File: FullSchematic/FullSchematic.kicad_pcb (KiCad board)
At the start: 2 copper layers, 91.4 x 81.3 mm, 59 parts, among them IC1 TTP223E-BA6, J1 USB_B_Micro, J2 TP4056, P1 Touch Pad, Q1 PMOS, U1 LM1117-3.3, U2 CH340C, U3 24LC64, U4 STM32F051C6T6

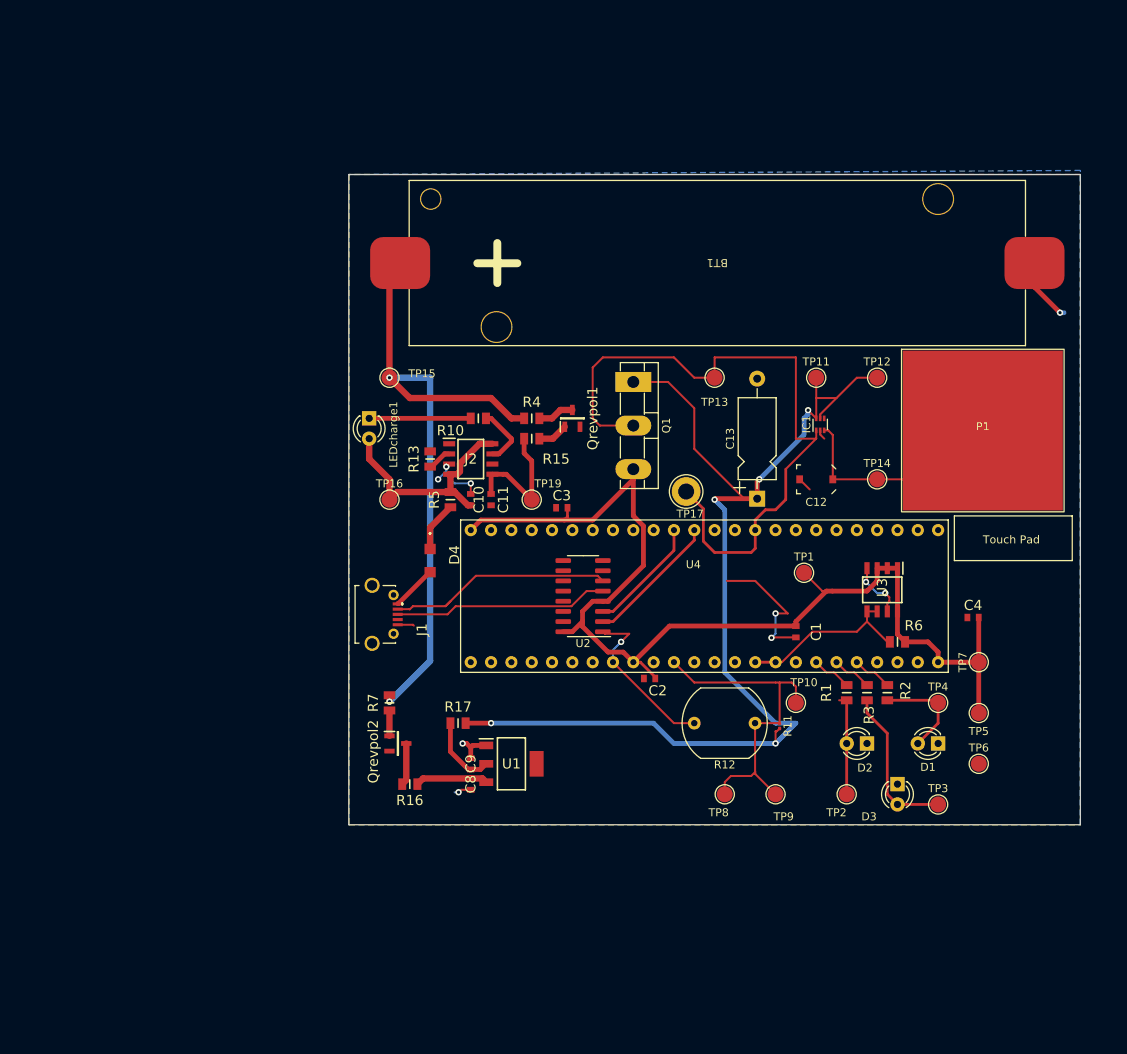
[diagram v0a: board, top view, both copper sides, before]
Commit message: Added uvlo circuit
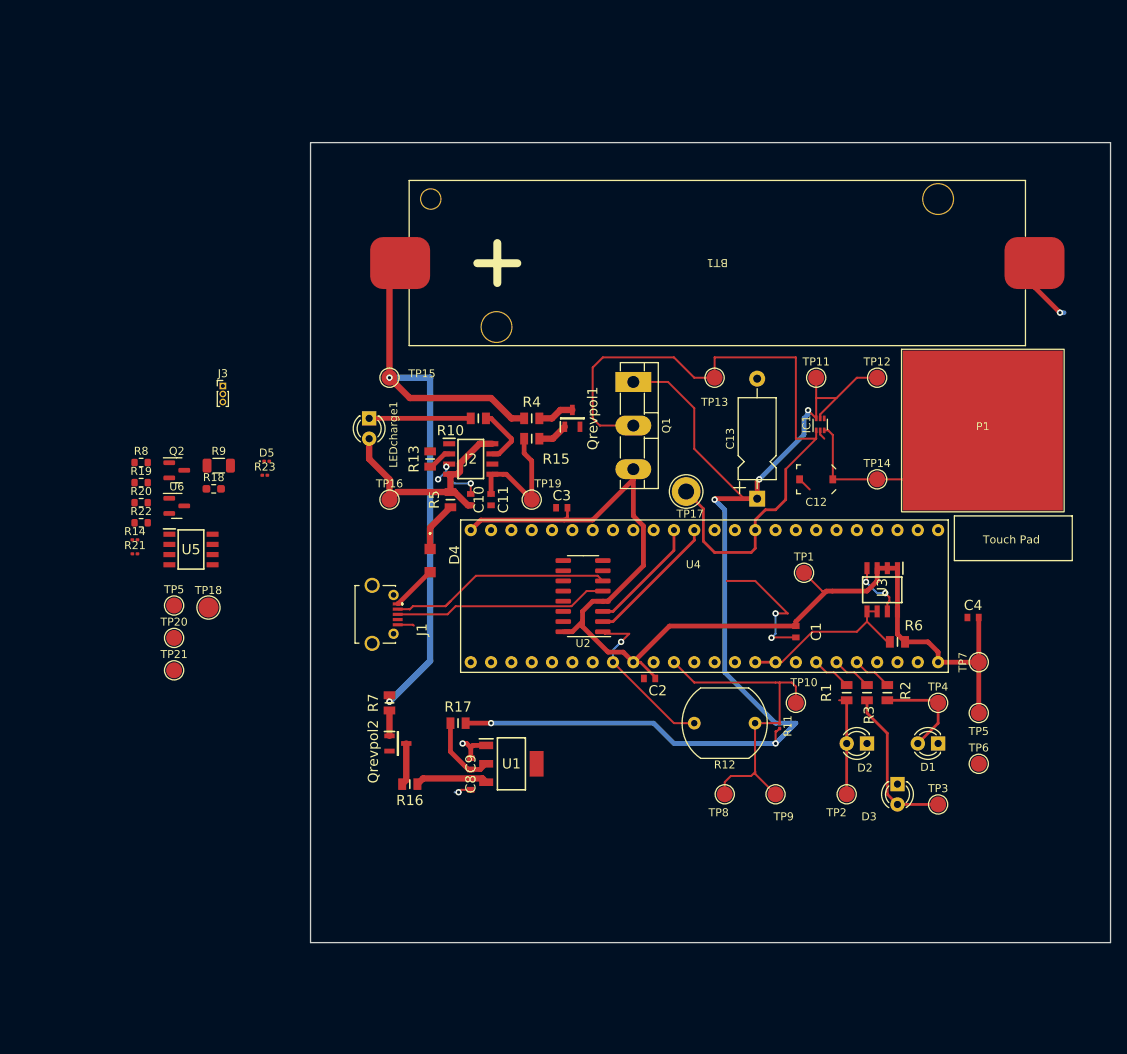
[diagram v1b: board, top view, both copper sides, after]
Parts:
- added D5: LED, LED_SMD:LED_0201_0603Metric, F.Cu at (71.0, 86.6)
- added J3: Conn_01x03_Pin, Connector_PinHeader_1.00mm:PinHeader_1x03_P1.00mm_Vertical, F.Cu at (65.5, 77.2)
- added Q2: IRLML6402, Package_TO_SOT_SMD:SOT-23, F.Cu at (59.8, 87.8)
- added R14: 1M, Resistor_SMD:R_0201_0603Metric, F.Cu at (54.5, 96.5)
- added R18: 10M, Resistor_SMD:R_0603_1608Metric_Pad0.98x0.95mm_HandSolder, F.Cu at (64.4, 90.1)
- added R19: 150k, Resistor_SMD:R_0603_1608Metric, F.Cu at (55.3, 89.3)
- added R20: 2.05M, Resistor_SMD:R_0603_1608Metric, F.Cu at (55.3, 91.8)
- added R21: 100k, Resistor_SMD:R_0201_0603Metric, F.Cu at (54.5, 98.2)
- added R22: 2M, Resistor_SMD:R_0603_1608Metric, F.Cu at (55.3, 94.3)
- added R23: 150, Resistor_SMD:R_0201_0603Metric, F.Cu at (70.8, 88.4)
- added R8: 2M, Resistor_SMD:R_0603_1608Metric, F.Cu at (55.3, 86.8)
- added R9: 2.5M, Resistor_SMD:R_1206_3216Metric, F.Cu at (65.0, 87.2)
- added TP18: TestPoint, TestPoint:TestPoint_Pad_D2.5mm, F.Cu at (63.7, 104.9)
- added TP20: TestPoint, TestPoint:TestPoint_Pad_D2.0mm, F.Cu at (59.4, 108.7)
- added TP21: TestPoint, TestPoint:TestPoint_Pad_D2.0mm, F.Cu at (59.4, 112.8)
- added TP5: TestPoint, TestPoint:TestPoint_Pad_D2.0mm, F.Cu at (59.4, 104.7)
- added U5: OP184, Library:SOIC127P600X175-8N, F.Cu at (61.5, 97.7)
- added U6: CJ432, Package_TO_SOT_SMD:SOT-23, F.Cu at (59.8, 92.2)
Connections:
- net /Microcontroller/Vbus renamed /Microcontroller/5V
- BT1 pad 2: 0 -> GND
- C9 pad 2: 0 -> GND
- Q1 pad 3: /Microcontroller/3.3V -> Net-(J3-Pin_1)
- R7 pad 1: /Power Module/Charging/Vbat -> /Power Module/Regulating/Vbat
- U1 pad 1: 0 -> GND
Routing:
- net GND: track 58.5 -> 71.1 mm, vias 8 -> 10
- net 0: track 14.8 -> 2.16 mm, vias 3 -> 1
- removed copper zone on B.Cu, net 0
- removed copper zone on F.Cu, net GND
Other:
- board size 91.4 x 81.3 mm -> 100 x 100 mm

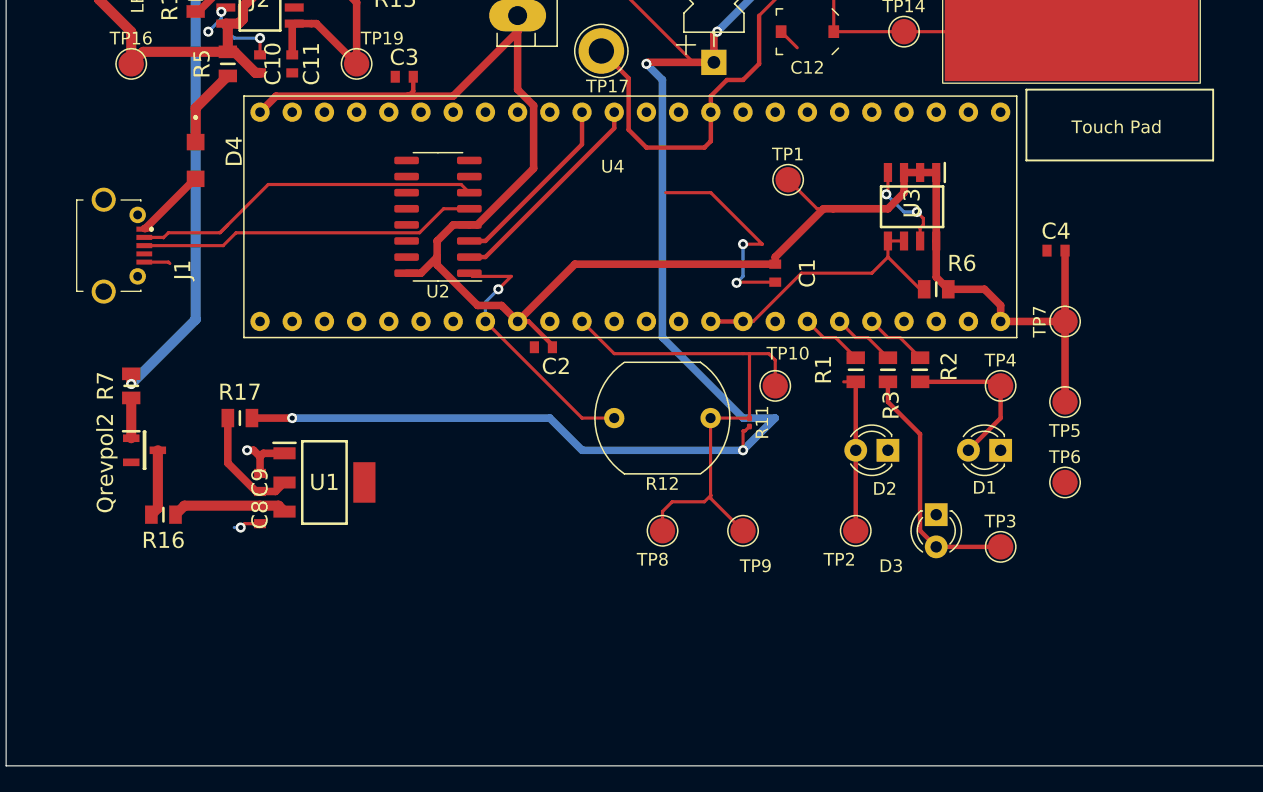
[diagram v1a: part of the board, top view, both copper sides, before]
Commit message: updated microcontroller BOM and added qr code to b.silk
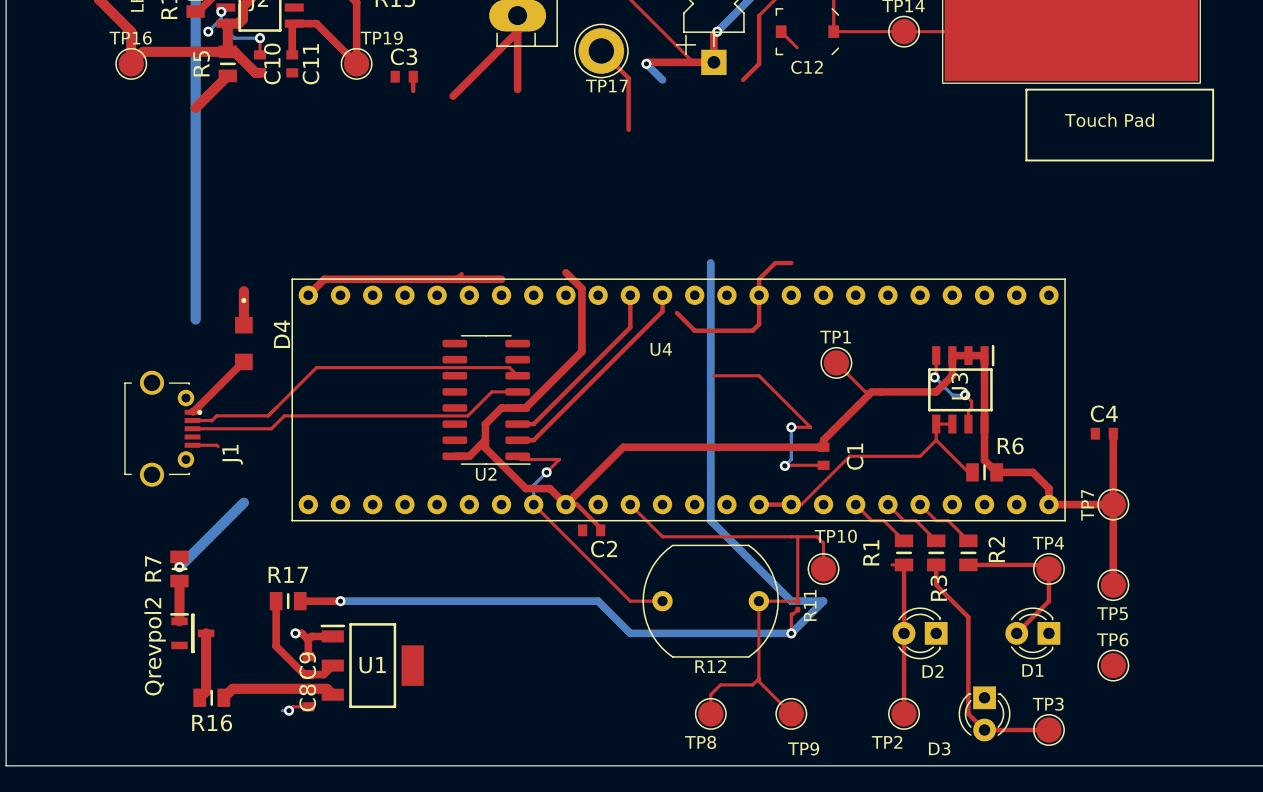
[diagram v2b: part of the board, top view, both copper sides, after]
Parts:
- moved TP3 14.9 mm to (158.8, 144.0)
- moved C4 14.9 mm to (163.1, 120.6)
- moved C9 14.9 mm to (100.3, 138.9)
- moved D1 14.9 mm to (158.8, 136.4)
- moved D2 14.9 mm to (149.9, 136.4)
- moved J1 14.9 mm to (88.0, 120.2)
- moved Qrevpol2 14.9 mm to (91.2, 136.4)
- moved TP5 14.9 mm to (163.8, 132.6)
- moved TP6 14.9 mm to (163.8, 138.9)
- moved U1 14.9 mm to (105.4, 138.9)
- moved U2 14.9 mm to (114.4, 118.0)
- moved R6 14.9 mm to (153.7, 123.7)
- moved U3 14.9 mm to (151.8, 117.2)
- moved C1 14.9 mm to (141.0, 122.4)
- moved C2 14.9 mm to (122.7, 128.2)
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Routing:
- net Net-(J3-Pin_1): track 0.00 -> 14.3 mm
- net /Microcontroller/3.3V: track 140.9 -> 126.6 mm
- net /Power Module/Regulating/Vbat: track 0.00 -> 7.98 mm, vias 0 -> 1
- net /Power Module/Charging/Vbat: track 82.3 -> 74.3 mm, vias 2 -> 1

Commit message: Confirmed part numbers and prices
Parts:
- removed C12: C_Variable, Capacitor_SMD:C_Trimmer_Murata_TZC3
- added C5: 20pF, Capacitor_THT:C_Disc_D4.7mm_W2.5mm_P5.00mm, F.Cu at (117.1, 94.7)
- added G***: LOGO, Library:QR-CODE, B.Cu at (137.2, 86.9)
- added J4: Conn_01x03_Pin, Connector_PinHeader_2.54mm:PinHeader_1x03_P2.54mm_Vertical, F.Cu at (53.7, 136.9)
- added Q3: IRLML6402, Package_TO_SOT_SMD:SOT-23, F.Cu at (115.7, 104.9)
- added Q4: 2N7002, Package_TO_SOT_SMD:SOT-23, F.Cu at (121.7, 104.8)
- C1, C2, C3, C4: footprint Library:CAPC1608X90N -> Capacitor_SMD:C_1206_3216Metric
- C10, C11, C8, C9: footprint Library:CAPC1608X90N -> Capacitor_SMD:C_0603_1608Metric
- C13: footprint Capacitor_THT:CP_Axial_L10.0mm_D4.5mm_P15.00mm_Horizontal -> Capacitor_THT:C_Disc_D4.3mm_W1.9mm_P5.00mm
- J3: footprint Connector_PinHeader_1.00mm:PinHeader_1x03_P1.00mm_Vertical -> Connector_PinHeader_2.54mm:PinHeader_1x03_P2.54mm_Vertical
- Q1: value PMOS -> IRLML6402; footprint Package_TO_SOT_THT:TO-3P-3_Vertical -> Package_TO_SOT_SMD:SOT-23
- R1, R2, R3: value 270 -> 270R; footprint Library:RESC2013X65N -> Resistor_SMD:R_1206_3216Metric
- R10, R13, R15, R16, R17, R4, R5, R7: footprint Library:RESC2013X65N -> Resistor_SMD:R_1206_3216Metric
- R12: footprint OptoDevice:R_LDR_10x8.5mm_P7.6mm_Vertical -> OptoDevice:R_LDR_5.0x4.1mm_P3mm_Vertical
- R14, R21: footprint Resistor_SMD:R_0201_0603Metric -> Resistor_SMD:R_0805_2012Metric
- R18: footprint Resistor_SMD:R_0603_1608Metric_Pad0.98x0.95mm_HandSolder -> Resistor_SMD:R_0805_2012Metric
- R19: footprint Resistor_SMD:R_0603_1608Metric -> Resistor_SMD:R_0402_1005Metric
- R20: footprint Resistor_SMD:R_0603_1608Metric -> Resistor_SMD:R_0805_2012Metric
- R23: value 150 -> 150R
- TP17: footprint TestPoint:TestPoint_Loop_D3.80mm_Drill2.0mm -> TestPoint:TestPoint_Keystone_5005-5009_Compact
- moved J3 86.5 mm to (147.7, 104.4)
- moved TP8 77.9 mm to (59.8, 113.8)
- moved R12 77.9 mm to (63.6, 104.9)
- moved TP10 77.9 mm to (68.7, 102.3)
- moved TP9 77.9 mm to (66.1, 113.8)
- moved R11 77.9 mm to (66.6, 105.2)
- moved TP5 76.2 mm to (92.3, 106.4)
- moved R23 47.3 mm to (117.0, 98.3)
- moved D5 44.7 mm to (114.1, 98.3)
- moved R22 43.4 mm to (95.8, 78.8), turned to 90 degrees
- moved R21 42.9 mm to (92.8, 78.8), turned to 90 degrees
- moved R20 36.9 mm to (89.7, 78.7), turned to 90 degrees
- moved R14 36.0 mm to (89.9, 102.9)
- moved TP21 35.3 mm to (72.5, 80.0)
- moved TP18 35.3 mm to (98.4, 98.3)
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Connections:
- net /Power Module/Vboard renamed /Vboard
- net Net-(J3-Pin_1) renamed /Pin 1
- C1 pad 1: /Microcontroller/3.3V -> Net-(J4-Pin_2)
- C8 pad 2: 0 -> GND
- IC1 pad 1: /Microcontroller/T_sensor -> /Output of Touch Sensor
- Q1 pad 2: /Microcontroller/T_sensor -> Net-(Q1-G)
- R23 pad 1: /Microcontroller/T_sensor -> /Output of Touch Sensor
- TP13 pad 1: /Microcontroller/T_sensor -> /Output of Touch Sensor
- TP17 pad 1: /Microcontroller/T_sensor -> /Output of Touch Sensor
- U2 pad 16: /Microcontroller/3.3V -> Net-(J4-Pin_2)
- U2 pad 4: /Microcontroller/3.3V -> Net-(J4-Pin_2)
- U4 pad 34: /Microcontroller/T_sensor -> /Output of Touch Sensor
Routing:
- net /Output of Touch Sensor: track 0.00 -> 105.2 mm
- net /Vboard: track 141.3 -> 238.2 mm, vias 5 -> 6
- net /Power Module/Regulating/Vbat: track 7.98 -> 99.7 mm, vias 1 -> 2
- net /Microcontroller/T_sensor: track 87.1 -> 0.00 mm
- net Net-(J4-Pin_2): track 0.00 -> 79.4 mm, vias 0 -> 3
- net Net-(R14-Pad2): track 0.00 -> 51.8 mm, vias 0 -> 4
- net /Microcontroller/LDR_sensor: track 42.6 -> 89.4 mm, vias 0 -> 1
- net /Microcontroller/3.3V: track 126.6 -> 172.3 mm, vias 0 -> 3
- net /Power Module/Charging/Vbat: track 74.3 -> 116.8 mm
- net GND: track 71.1 -> 28.8 mm, vias 10 -> 7
- net Net-(U5-+): track 0.00 -> 42.2 mm, vias 0 -> 4
- net /Pin 1: track 14.3 -> 48.6 mm, vias 0 -> 1
- net Net-(U6-A): track 0.00 -> 17.8 mm, vias 0 -> 2
- net Net-(Q1-G): track 0.00 -> 14.0 mm, vias 0 -> 2
- net /Microcontroller/5V: track 5.68 -> 19.3 mm
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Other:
- board text added: "3.3V"
- board text added: "5V"
- board text added: "Bypass CMOS config"
- board text added: "CMOS config"
- board text added: "Group 14 Git link SMNAIM002 JHNASH009 KDZKUD001"

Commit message: corrected connection
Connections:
- R18 pad 2: GND -> Net-(U6-A)
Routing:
- net Net-(U6-A): track 17.8 -> 22.0 mm
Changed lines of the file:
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@@
   (net 87 "unconnected-(U5-NC-Pad5)")
   (net 88 "unconnected-(U5-VOS-Pad8)")
-  (net 89 "Net-(J4-Pin_2)")
+  (net 89 "Net-(#FLG05-pwr)")
   (net 90 "Net-(Q1-G)")
   (footprint "TestPoint:TestPoint_Pad_D2.0mm" (layer "F.Cu")
@@
       (net 27 "/Microcontroller/Tx") (pinfunction "RXD") (pintype "input"))
     (pad "4" smd roundrect (at -2.475 -0.635 180) (size 1.95 0.6) (layers "F.Cu" "F.Paste" "F.Mask") (roundrect_rratio 0.25)
-      (net 89 "Net-(J4-Pin_2)") (pinfunction "V3") (pintype "passive"))
+      (net 89 "Net-(#FLG05-pwr)") (pinfunction "V3") (pintype "passive"))
     (pad "5" smd roundrect (at -2.475 0.635 180) (size 1.95 0.6) (layers "F.Cu" "F.Paste" "F.Mask") (roundrect_rratio 0.25)
       (net 17 "Net-(J1-D+)") (pinfunction "UD+") (pintype "bidirectional"))
@@
       (net 40 "unconnected-(U2-R232-Pad15)") (pinfunction "R232") (pintype "input+no_connect"))
     (pad "16" smd roundrect (at 2.475 -4.445 180) (size 1.95 0.6) (layers "F.Cu" "F.Paste" "F.Mask") (roundrect_rratio 0.25)
-      (net 89 "Net-(J4-Pin_2)") (pinfunction "VCC") (pintype "power_in"))
+      (net 89 "Net-(#FLG05-pwr)") (pinfunction "VCC") (pintype "power_in"))
     (model "${KICAD6_3DMODEL_DIR}/Package_SO.3dshapes/SOIC-16_3.9x9.9mm_P1.27mm.wrl"
       (offset (xyz 0 0 0))
@@
       (stroke (width 0.1) (type solid)) (layer "F.Fab"))
     (pad "1" smd roundrect (at -1.475 0 270) (size 1.15 1.8) (layers "F.Cu" "F.Paste" "F.Mask") (roundrect_rratio 0.217391)
-      (net 89 "Net-(J4-Pin_2)") (pintype "passive"))
+      (net 89 "Net-(#FLG05-pwr)") (pintype "passive"))
     (pad "2" smd roundrect (at 1.475 0 270) (size 1.15 1.8) (layers "F.Cu" "F.Paste" "F.Mask") (roundrect_rratio 0.217391)
       (net 3 "GND") (pintype "passive"))
@@
       (net 83 "Net-(R14-Pad2)") (pintype "passive"))
     (pad "2" smd roundrect (at 0.9125 0 90) (size 1.025 1.4) (layers "F.Cu" "F.Paste" "F.Mask") (roundrect_rratio 0.243902)
-      (net 3 "GND") (pintype "passive"))
+      (net 84 "Net-(U6-A)") (pintype "passive"))
     (model "${KICAD6_3DMODEL_DIR}/Resistor_SMD.3dshapes/R_0805_2012Metric.wrl"
       (offset (xyz 0 0 0))
@@
       (net 2 "/Microcontroller/3.3V") (pinfunction "Pin_1") (pintype "passive"))
     (pad "2" thru_hole oval (at 0 2.54 180) (size 1.7 1.7) (drill 1) (layers "*.Cu" "*.Mask")
-      (net 89 "Net-(J4-Pin_2)") (pinfunction "Pin_2") (pintype "passive"))
+      (net 89 "Net-(#FLG05-pwr)") (pinfunction "Pin_2") (pintype "passive"))
     (pad "3" thru_hole oval (at 0 5.08 180) (size 1.7 1.7) (drill 1) (layers "*.Cu" "*.Mask")
       (net 13 "/Microcontroller/5V") (pinfunction "Pin_3") (pintype "passive"))
@@
   (segment (start 94.824 101.331) (end 95.84 100.315) (width 0.35) (layer "B.Cu") (net 83))
   (segment (start 100.412 94.727) (end 101.428 95.743) (width 0.35) (layer "B.Cu") (net 83))
-  (segment (start 84.664 79.995) (end 86.188 79.995) (width 0.35) (layer "F.Cu") (net 84))
+  (segment (start 85.344 79.995) (end 86.188 79.995) (width 0.35) (layer "F.Cu") (net 84))
   (segment (start 86.188 79.995) (end 86.696 79.487) (width 0.35) (layer "F.Cu") (net 84))
+  (segment (start 83.6225 78.232) (end 85.344 78.232) (width 0.25) (layer "F.Cu") (net 84))
+  (segment (start 85.344 78.232) (end 85.344 79.995) (width 0.25) (layer "F.Cu") (net 84))
   (segment (start 91.268 90.663) (end 93.3 88.631) (width 0.35) (layer "F.Cu") (net 84))
+  (segment (start 83.14 77.7495) (end 83.6225 78.232) (width 0.25) (layer "F.Cu") (net 84))
+  (segment (start 84.664 79.995) (end 85.344 79.995) (width 0.35) (layer "F.Cu") (net 84))
   (segment (start 90.76 90.663) (end 91.268 90.663) (width 0.35) (layer "F.Cu") (net 84))
   (via (at 93.3 88.631) (size 0.8) (drill 0.4) (layers "F.Cu" "B.Cu") (net 84))

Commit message: Checked part #s, prices, footprints
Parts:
- added D6: Schottky - 0.21@1A, Library:Schottky Diode, F.Cu at (55.4, 34.8)
- added J5: Conn_01x03_Pin, Connector_PinHeader_2.54mm:PinHeader_1x03_P2.54mm_Vertical, F.Cu at (49.0, 34.4)
- added TP22: TestPoint, TestPoint:TestPoint_Pad_D2.0mm, F.Cu at (63.5, 34.0)
- added TP23: TestPoint, TestPoint:TestPoint_Pad_D2.0mm, F.Cu at (63.5, 38.1)
- D4: value 1N5819 -> Schottky - 0.21@1A; footprint Library:Temp Schottky -> Library:Schottky Diode
- LEDcharge1: footprint LED_THT:LED_D3.0mm_IRBlack -> LED_SMD:LED_0603_1608Metric
- moved D4 21.5 mm to (55.9, 104.1)
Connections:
- R4 pad 1: /Power Module/Charging/Vbat -> Net-(J5-Pin_1)
- TP15 pad 1: /Power Module/Charging/Vbat -> Net-(J5-Pin_1)
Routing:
- net Net-(LEDcharge1-K): track 12.7 -> 0.00 mm
- net /Power Module/Charging/Vin: track 29.8 -> 21.1 mm

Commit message: Final Board
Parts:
- U1: footprint Library:SOT230P700X180-4N -> Package_TO_SOT_SMD:SOT-223
- moved TP22 112.5 mm to (91.2, 143.1)
- moved TP23 107.9 mm to (111.0, 135.0)
- moved D6 54.2 mm to (54.2, 89.0), turned to -90 degrees
- moved J5 41.0 mm to (54.0, 75.0)
- moved C9 1.53 mm to (73.3, 142.4)
- moved C8 1.48 mm to (73.3, 146.4)
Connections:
- P1 pad Touch Pad1: (no net) -> Net-(IC1-I)
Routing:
- net GND: track 28.8 -> 104.0 mm, vias 7 -> 28
- net Net-(J5-Pin_1): track 0.00 -> 51.7 mm, vias 0 -> 3
- net Net-(D6-A): track 3.80 -> 35.1 mm, vias 0 -> 2
- net /Power Module/Regulating/Vin: track 8.63 -> 29.7 mm
- net /Microcontroller/5V: track 19.3 -> 36.3 mm
- net /Power Module/Charging/Vbat: track 116.8 -> 101.6 mm, vias 1 -> 0
- net Net-(R22-Pad2): track 0.00 -> 13.5 mm, vias 0 -> 2
- net Net-(LEDcharge1-K): track 0.00 -> 12.5 mm
- net Net-(D4-K): track 3.59 -> 14.7 mm
- net /Power Module/Charging/Vin: track 21.1 -> 31.5 mm
- net /Vboard: track 238.2 -> 247.2 mm, vias 6 -> 8
- net Net-(D6-K): track 0.00 -> 6.76 mm
- net /Microcontroller/LDR_sensor: track 89.4 -> 85.2 mm, vias 1 -> 2
- net Net-(U5--): track 12.7 -> 16.7 mm
- net Net-(IC1-I): track 33.0 -> 35.1 mm
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- added copper zone on F.Cu, net (none)
- added copper zone on B.Cu, net GND
- added copper zone on F.Cu, net GND
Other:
- outline, holes or cut-outs redrawn
